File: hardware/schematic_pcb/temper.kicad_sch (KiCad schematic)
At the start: 40 parts, among them J1 conn_01x03, J2 conn_01x03, J3 conn_01x03, J4 conn_01x03, J5 Charge Connector, J6 MCU Serial I/F, J7 Conn_01x08, M1 DMP3099L-7, Q1 2N7002, SW1 Reset, SW2 Factory Reset, SW3 ON/OFF, U1 MCP9700, U2 ESP32-WROOM-32

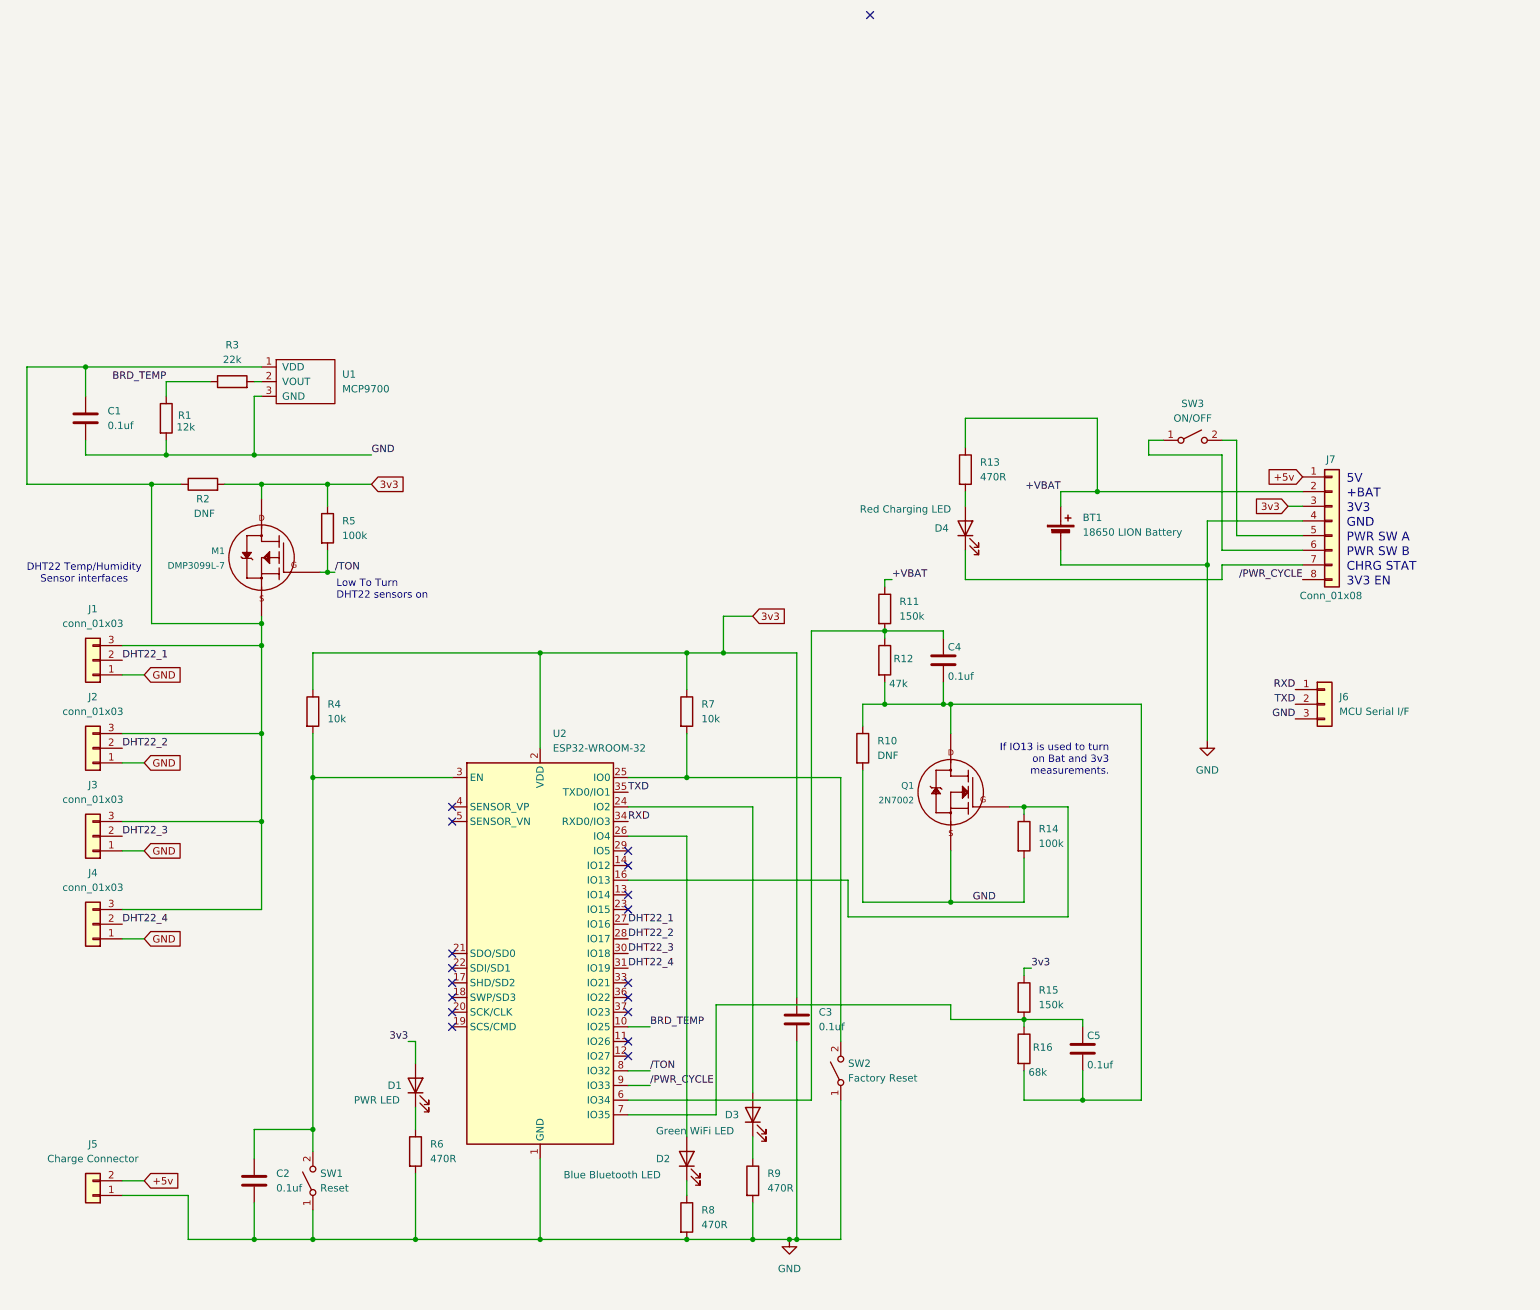
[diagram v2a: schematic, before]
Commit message: - Move ADC2 pins as ADC2 cannot be used with WiFi. - Add power up reset controller to ensure MCU boots after powercyle event.
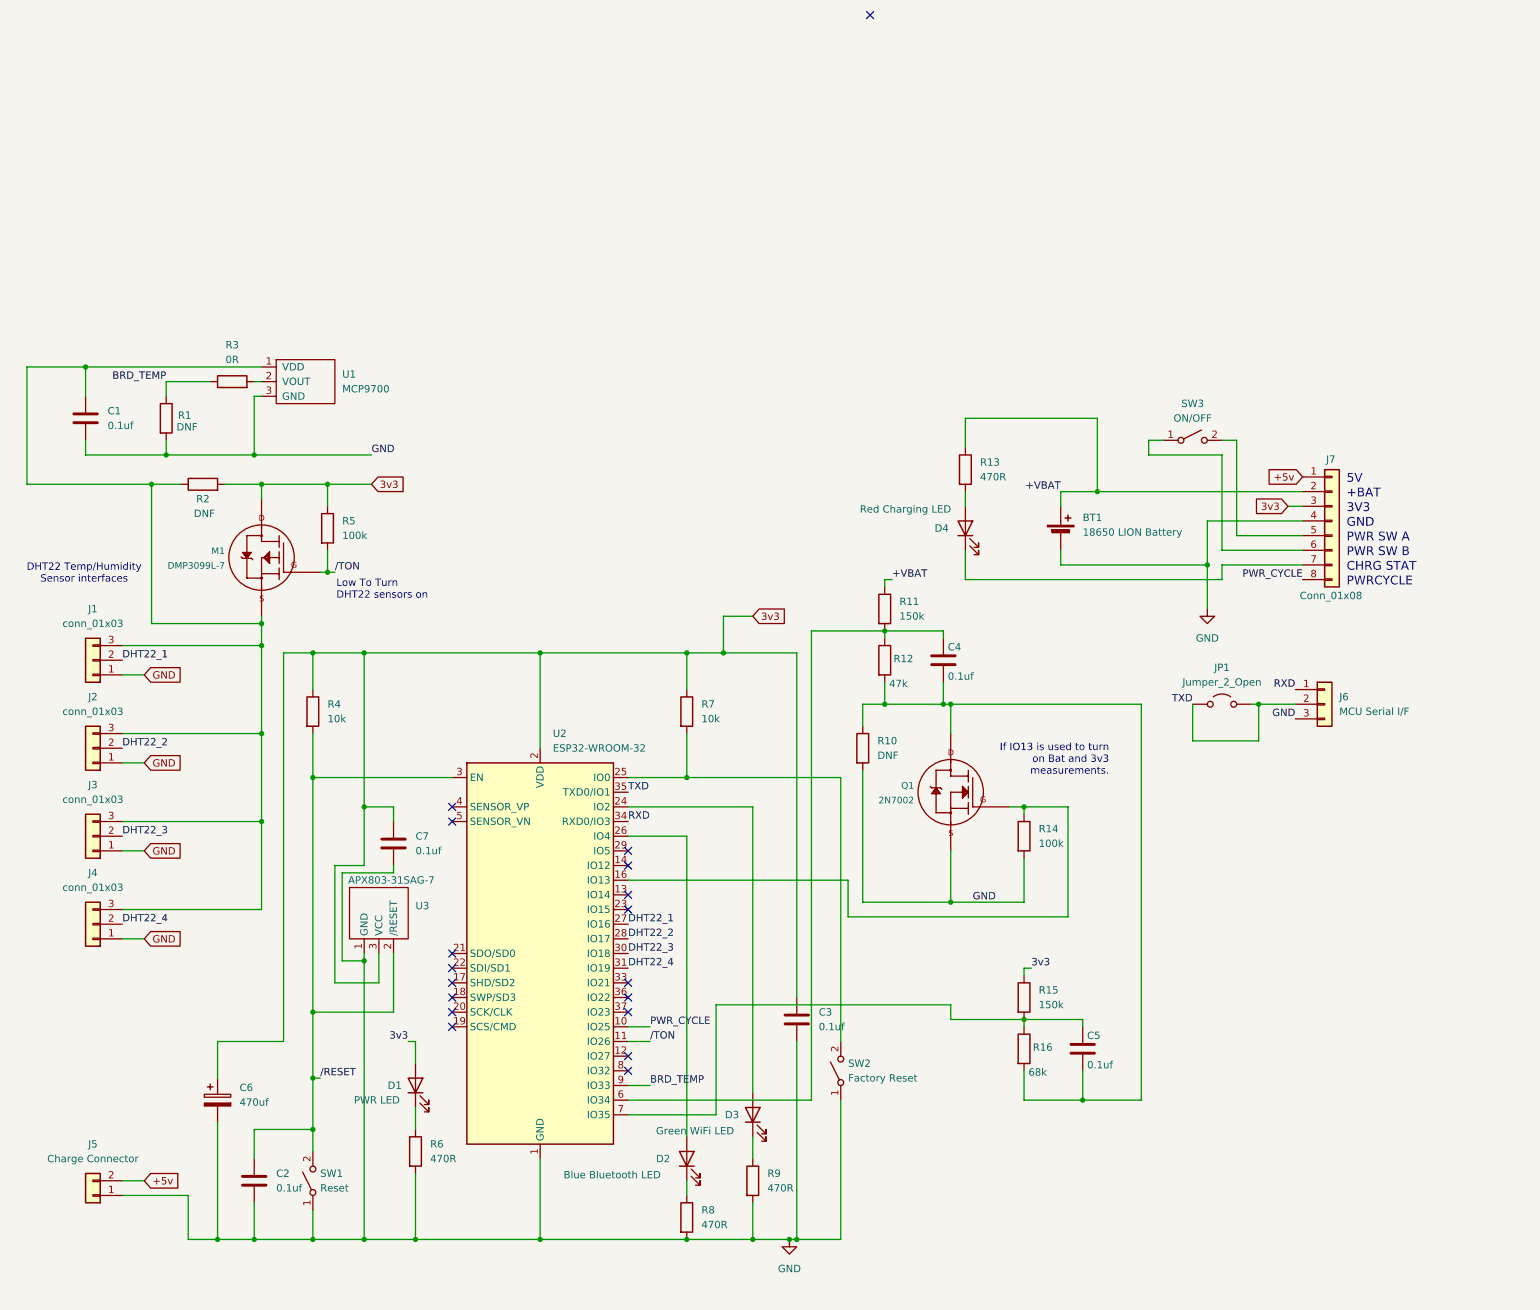
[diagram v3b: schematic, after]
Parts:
- added C6: 470uf, Capacitor_THT:CP_Radial_D6.3mm_P2.50mm, symbol Device:C_Polarized
- added C7: 0.1uf, Capacitor_SMD:C_0603_1608Metric, symbol Device:C
- added JP1: Jumper_2_Open, Connector_PinHeader_2.54mm:PinHeader_1x02_P2.54mm_Vertical, symbol Jumper:Jumper_2_Open
- added U3: APX803-31SAG-7, Package_TO_SOT_SMD:SOT-23, symbol pja_1:APX803-31SAG-7
- R1: value 12k -> DNF
- R3: value 22k -> 0R
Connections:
- net 3v3: now also C6.1, C7.1, U3.3 (VCC)
- net BRD_TEMP: now also U2.9 (IO33); no longer U2.10 (IO25)
- net GND: now also C6.2, C7.2, U3.1 (GND)
- net TXD: now also JP1.1 (A), JP1.2 (B)
- net /TON: now also U2.11 (IO26); no longer U2.8 (IO32)
- net /RESET: now reaches C2.1, R4.2, SW1.2 (B), U2.3 (EN)
- net /RESET: now also U3.2 (/RESET)
- net /PWR_CYCLE renamed PWR_CYCLE
- net PWR_CYCLE: now also U2.10 (IO25); no longer U2.9 (IO33)
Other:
- note added: "PWRCYCLE"
- note removed: "3V3 EN"

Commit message: Bump PCB to V1.4 to accept the 26700 Sodium ION battery.
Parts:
- BT1: footprint PJA_Connectors:18650_battery_holder -> PJA_Connectors:18650_26700_battery_holder
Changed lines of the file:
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@@
 			)
 		)
-		(property "Footprint" "PJA_Connectors:18650_battery_holder"
+		(property "Footprint" "PJA_Connectors:18650_26700_battery_holder"
 			(at 200.66 59.436 90)
 			(effects

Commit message: Add 1.5 HW design.
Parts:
- removed J7: Conn_01x08, Connector_PinHeader_2.54mm:PinHeader_1x08_P2.54mm_Vertical, symbol Connector_Generic:Conn_01x08
- removed U3: APX803-31SAG-7, Package_TO_SOT_SMD:SOT-23, symbol pja_1:APX803-31SAG-7
- added J7: Conn_01x10, Connector_PinHeader_2.54mm:PinHeader_1x10_P2.54mm_Vertical, symbol Connector_Generic:Conn_01x10
- added JP2: Jumper_2_Bridged, Jumper:SolderJumper-2_P1.3mm_Bridged_RoundedPad1.0x1.5mm, symbol Jumper:Jumper_2_Bridged
- added Q2: 2N7002, Package_TO_SOT_SMD:SOT-23-3, symbol pja_1:2N7002
- added R17: 100k, Resistor_SMD:R_0402_1005Metric_Pad0.72x0.64mm_HandSolder, symbol Device:R
- C1: footprint Capacitor_SMD:C_0603_1608Metric -> Capacitor_SMD:C_0402_1005Metric_Pad0.74x0.62mm_HandSolder; LCSC (none) -> C307331
- C2: renamed from C6; value 470uf -> DNF
- C3: renamed from C2; footprint Capacitor_SMD:C_0603_1608Metric -> Capacitor_SMD:C_0402_1005Metric_Pad0.74x0.62mm_HandSolder; LCSC (none) -> C307331
- C4: renamed from C3; footprint Capacitor_SMD:C_0603_1608Metric -> Capacitor_SMD:C_0402_1005Metric_Pad0.74x0.62mm_HandSolder; LCSC (none) -> C307331
- C5: renamed from C4; footprint Capacitor_SMD:C_0603_1608Metric -> Capacitor_SMD:C_0402_1005Metric_Pad0.74x0.62mm_HandSolder; LCSC (none) -> C307331
- C6: renamed from C5; footprint Capacitor_SMD:C_0603_1608Metric -> Capacitor_SMD:C_0402_1005Metric_Pad0.74x0.62mm_HandSolder; LCSC (none) -> C307331
- C7: value 0.1uf -> 22uf; footprint Capacitor_SMD:C_0603_1608Metric -> Capacitor_SMD:C_1206_3216Metric_Pad1.33x1.80mm_HandSolder; LCSC (none) -> C12891
- D1: renamed from D2; footprint LED_SMD:LED_1206_3216Metric -> LED_SMD:LED_0805_2012Metric_Pad1.15x1.40mm_HandSolder; LCSC (none) -> C2296
- D2: renamed from D3; value Green WiFi LED -> GreenLED; footprint LED_SMD:LED_1206_3216Metric -> LED_SMD:LED_0805_2012Metric_Pad1.15x1.40mm_HandSolder; LCSC (none) -> C2297
- D3: renamed from D4; footprint LED_SMD:LED_1206_3216Metric -> LED_SMD:LED_0805_2012Metric_Pad1.15x1.40mm_HandSolder; LCSC (none) -> C84256
- D4: renamed from D1; value PWR LED -> GreenLED; footprint LED_SMD:LED_1206_3216Metric -> LED_SMD:LED_0805_2012Metric_Pad1.15x1.40mm_HandSolder; LCSC (none) -> C2297
- M1: value DMP3099L-7 -> AO3401A; LCSC (none) -> C15127
- Q1: LCSC (none) -> C8545
- R1, R2: footprint Resistor_SMD:R_0603_1608Metric_Pad0.98x0.95mm_HandSolder -> Resistor_SMD:R_0402_1005Metric_Pad0.72x0.64mm_HandSolder
- R10: renamed from R11; value 150k -> 100k; footprint Resistor_SMD:R_0603_1608Metric_Pad0.98x0.95mm_HandSolder -> Resistor_SMD:R_0402_1005Metric_Pad0.72x0.64mm_HandSolder; LCSC (none) -> C25741
- R11: renamed from R12; value 47k -> 22k; footprint Resistor_SMD:R_0603_1608Metric_Pad0.98x0.95mm_HandSolder -> Resistor_SMD:R_0402_1005Metric_Pad0.72x0.64mm_HandSolder; LCSC (none) -> C25768
- R12: renamed from R13; footprint Resistor_SMD:R_0603_1608Metric_Pad0.98x0.95mm_HandSolder -> Resistor_SMD:R_0402_1005Metric_Pad0.72x0.64mm_HandSolder; LCSC (none) -> C23179
- R13: renamed from R14; footprint Resistor_SMD:R_0603_1608Metric_Pad0.98x0.95mm_HandSolder -> Resistor_SMD:R_0402_1005Metric_Pad0.72x0.64mm_HandSolder; LCSC (none) -> C25741
- R14: renamed from R15; value 150k -> 100k; footprint Resistor_SMD:R_0603_1608Metric_Pad0.98x0.95mm_HandSolder -> Resistor_SMD:R_0402_1005Metric_Pad0.72x0.64mm_HandSolder; LCSC (none) -> C25741
- R15: renamed from R16; value 68k -> 47k; footprint Resistor_SMD:R_0603_1608Metric_Pad0.98x0.95mm_HandSolder -> Resistor_SMD:R_0402_1005Metric_Pad0.72x0.64mm_HandSolder; LCSC (none) -> C25792
- R16: renamed from R6; footprint Resistor_SMD:R_0603_1608Metric_Pad0.98x0.95mm_HandSolder -> Resistor_SMD:R_0402_1005Metric_Pad0.72x0.64mm_HandSolder; LCSC (none) -> C23179
- R3: footprint Resistor_SMD:R_0603_1608Metric_Pad0.98x0.95mm_HandSolder -> Resistor_SMD:R_0402_1005Metric_Pad0.72x0.64mm_HandSolder; LCSC (none) -> C17168
- R4: footprint Resistor_SMD:R_0603_1608Metric_Pad0.98x0.95mm_HandSolder -> Resistor_SMD:R_0402_1005Metric_Pad0.72x0.64mm_HandSolder; LCSC (none) -> C25744
- R5: footprint Resistor_SMD:R_0603_1608Metric_Pad0.98x0.95mm_HandSolder -> Resistor_SMD:R_0402_1005Metric_Pad0.72x0.64mm_HandSolder; LCSC (none) -> C25741
- R6: renamed from R7; footprint Resistor_SMD:R_0603_1608Metric_Pad0.98x0.95mm_HandSolder -> Resistor_SMD:R_0402_1005Metric_Pad0.72x0.64mm_HandSolder; LCSC (none) -> C25744
- R7: renamed from R8; footprint Resistor_SMD:R_0603_1608Metric_Pad0.98x0.95mm_HandSolder -> Resistor_SMD:R_0402_1005Metric_Pad0.72x0.64mm_HandSolder; LCSC (none) -> C23179
- R8: renamed from R9; footprint Resistor_SMD:R_0603_1608Metric_Pad0.98x0.95mm_HandSolder -> Resistor_SMD:R_0402_1005Metric_Pad0.72x0.64mm_HandSolder; LCSC (none) -> C23179
- R9: renamed from R10; footprint Resistor_SMD:R_0603_1608Metric_Pad0.98x0.95mm_HandSolder -> Resistor_SMD:R_0402_1005Metric_Pad0.72x0.64mm_HandSolder
- SW1: value Reset -> tactsw; footprint PJA_Switches:switch_SPST_5mmx3mmx2.5mm -> Button_Switch_SMD:SW_SPST_SKQG_WithoutStem; LCSC (none) -> C318884
- SW2: value Factory Reset -> tactsw; footprint PJA_Switches:switch_SPST_5mmx3mmx2.5mm -> Button_Switch_SMD:SW_SPST_SKQG_WithoutStem; LCSC (none) -> C318884
- SW3: value ON/OFF -> tactsw; footprint PJA_Switches:switch_SPST_5mmx3mmx2.5mm -> Button_Switch_SMD:SW_SPST_SKQG_WithoutStem; LCSC (none) -> C318884
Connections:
- net +5v: now also J7.1 (Pin_1)
- net +VBAT: now also J7.2 (Pin_2)
- net 3v3: now also J7.3 (Pin_3), R17.1
- net GND: now also J7.4 (Pin_4), Q2.2 (S); no longer R16.2
- net PWR_CYCLE: now also J7.8 (Pin_8)
- net TXD: now also JP2.1 (A); no longer J6.2 (Pin_2), JP1.2 (B)
- net /RESET: now also J7.10 (Pin_10)
- net CHRG_STAT: now reaches D3.1 (K)
- net CHRG_STAT: now also J7.7 (Pin_7)
- net PWR_SW_B: now reaches SW3.1 (A)
- net PWR_SW_B: now also J7.6 (Pin_6)
- net PWR_SW_A: now reaches SW3.2 (B)
- net PWR_SW_A: now also J7.5 (Pin_5)
- net /CHRG_OFF: now reaches U2.33 (IO21)
- net /CHRG_OFF: now also J7.9 (Pin_9)
- net /DIS_PWR_LED: now reaches U2.36 (IO22)
- net /DIS_PWR_LED: now also Q2.1 (G), R17.2
- new net: Q2.3 (D), R16.2
- new net: J6.2 (Pin_2), JP1.2 (B), JP2.2 (B)
- no-connect marks 18 -> 16
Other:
- note added: "/CHRG_OFF"
- note added: "/RESET"
- note added: "FACTORY DEFAULTS"
- note added: "ON/OFF"
- note added: "Parts not fitted by JCLPCB - U1 - U2 - C2 - J1 - J2 - J3 - J4 - J5 - J6 - J7 - Battery holder and battery"
- note added: "Power"
- note added: "RESET"
- note added: "WiFi"
- moved on the sheet: C4, D4, R16

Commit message: Update to add D5.
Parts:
- added D5: 1N5819, Diode_SMD:D_SMA_Handsoldering, symbol Diode:1N5819
- added F1: 3A, PJA_Fuses:PTC_23mm_3mm_10.2mm_wire_spacing, symbol Device:Polyfuse
- added F2: DNF, PJA_Fuses:Scherter_OMT125, symbol Device:Fuse
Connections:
- net +5v: now also D5.2 (A)
- net +VBAT: now also D5.1 (K), F1.1, F2.1; no longer BT1.1 (+)
- new net: BT1.1 (+), F1.2, F2.2
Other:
- note added: "D5 is fitted only if the 5V connector is actually connected to an external LION cell charger. In this case the usb battery power module connected to J7 should not have U1 fitted."
- note added: "This maybe an external 5V input (I.E from a USB connector). Or it may be connected to an external LION cell charger providing 4.2V Max to charge a LION cell."

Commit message: Update JCLPCB not fitted parts.
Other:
- note added: "Parts not fitted by JCLPCB - D5 - U1 - U2 Optional parts - C2 - J1 - J2 - J3 - J4 - J5 - J6 - J7 - Battery holder and battery"
- note removed: "Parts not fitted by JCLPCB - U1 - U2 - C2 - J1 - J2 - J3 - J4 - J5 - J6 - J7 - Battery holder and battery"
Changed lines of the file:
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@@
 		)
 	)
-	(text "Parts not fitted by JCLPCB\n- U1\n- U2\n- C2\n- J1\n- J2\n- J3\n- J4\n- J5\n- J6\n- J7\n- Battery holder and battery\n"
+	(text "Parts not fitted by JCLPCB\n- D5\n- U1\n- U2\n\nOptional parts\n- C2\n- J1\n- J2\n- J3\n- J4\n- J5\n- J6\n- J7\n- Battery holder and battery\n"
 		(exclude_from_sim no)
 		(at 115.316 40.386 0)

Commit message: Added cap on DHT22 power. It's unclear if this is needed and these PCB's have not been built as I'm testing the 1.7 PCB to check if the 220uf 25v cap fixes the sensor read lockup for sensors 2 & 3.
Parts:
- added C8: 100uf 16v, Capacitor_THT:CP_Radial_D5.0mm_P2.50mm, symbol Device:C_Polarized
- C2: value DNF -> 220uf 25v
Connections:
- net GND: now also C8.2
- net at C1.1, J1.3 (Pin_3), J2.3 (Pin_3)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: now also C8.1
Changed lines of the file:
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@@
 	)
 	(junction
+		(at 50.8 125.73)
+		(diameter 0)
+		(color 0 0 0 0)
+	)
+	(junction
 		(at 200.66 40.64)
 		(diameter 0)
@@
 	)
 	(junction
+		(at 50.8 182.88)
+		(diameter 0)
+		(color 0 0 0 0)
+	)
+	(junction
 		(at 31.75 31.75)
 		(diameter 0)
@@
 	(wire
 		(pts
+			(xy 50.8 125.73) (xy 50.8 134.62)
+		)
+		(stroke
+			(width 0)
+			(type default)
+		)
+	)
+	(wire
+		(pts
 			(xy 219.71 97.79) (xy 218.44 97.79)
 		)
@@
 	(wire
 		(pts
-			(xy 54.61 182.88) (xy 49.53 182.88)
+			(xy 50.8 125.73) (xy 62.23 125.73)
+		)
+		(stroke
+			(width 0)
+			(type default)
+		)
+	)
+	(wire
+		(pts
+			(xy 54.61 182.88) (xy 50.8 182.88)
 		)
 		(stroke
@@
 	(wire
 		(pts
-			(xy 38.1 125.73) (xy 62.23 125.73)
+			(xy 38.1 125.73) (xy 50.8 125.73)
 		)
 		(stroke
@@
 	(wire
 		(pts
+			(xy 50.8 142.24) (xy 50.8 182.88)
+		)
+		(stroke
+			(width 0)
+			(type default)
+		)
+	)
+	(wire
+		(pts
 			(xy 135.89 102.87) (xy 162.56 102.87)
 		)
@@
 	(wire
 		(pts
+			(xy 50.8 182.88) (xy 49.53 182.88)
+		)
+		(stroke
+			(width 0)
+			(type default)
+		)
+	)
+	(wire
+		(pts
 			(xy 38.1 80.01) (xy 62.23 80.01)
 		)
@@
 	)
 	(symbol
+		(lib_id "Device:C_Polarized")
+		(at 50.8 138.43 0)
+		(unit 1)
+		(exclude_from_sim no)
+		(in_bom yes)
+		(on_board yes)
+		(dnp no)
+		(fields_autoplaced yes)
+		(property "Reference" "C8"
+			(at 54.61 136.2709 0)
+			(effects
+				(font
+					(size 1.27 1.27)
+				)
+				(justify left)
+			)
+		)
+		(property "Value" "100uf 16v"
+			(at 54.61 138.8109 0)
+			(effects
+				(font
+					(size 1.27 1.27)
+				)
+				(justify left)
+			)
+		)
+		(property "Footprint" "Capacitor_THT:CP_Radial_D5.0mm_P2.50mm"
+			(at 51.7652 142.24 0)
+			(effects
+				(font
+					(size 1.27 1.27)
+				)
+				(hide yes)
+			)
+		)
+		(property "Datasheet" "~"
+			(at 50.8 138.43 0)
+			(effects
+				(font
+					(size 1.27 1.27)
+				)
+				(hide yes)
+			)
+		)
+		(property "Description" "Polarized capacitor"
+			(at 50.8 138.43 0)
+			(effects
+				(font
+					(size 1.27 1.27)
+				)
+				(hide yes)
+			)
+		)
+		(pin "1"
+		)
+		(pin "2"
+		)
+		(instances
+			(project "temper"
+				(path "/ad9b79b0-4738-4cc8-a254-afb39ba62b16"
+					(reference "C8")
+					(unit 1)
+				)
+			)
+		)
+	)
+	(symbol
 		(lib_id "pja_1:2N7002")
 		(at 181.61 105.41 0)
@@
 			)
 		)
-		(property "Value" "DNF"
+		(property "Value" "220uf 25v"
 			(at 58.42 159.1309 0)
 			(effects
